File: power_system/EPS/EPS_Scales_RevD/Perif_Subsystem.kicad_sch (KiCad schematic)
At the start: 43 parts, among them CN1 DF11-16DP-2DSA(08), U12 TPS1HB08BQPWPRQ1, U13 LT8612EUDE#PBF, U16 INA260AIPWR

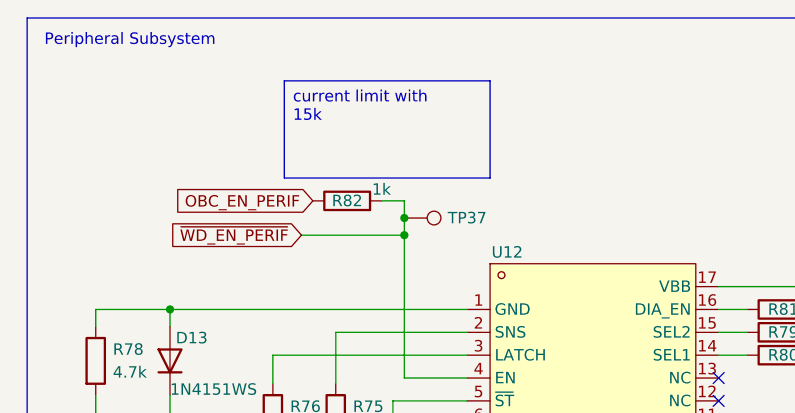
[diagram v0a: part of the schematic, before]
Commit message: Updated Project History
RevA through RevD directly accessible to see project revisions
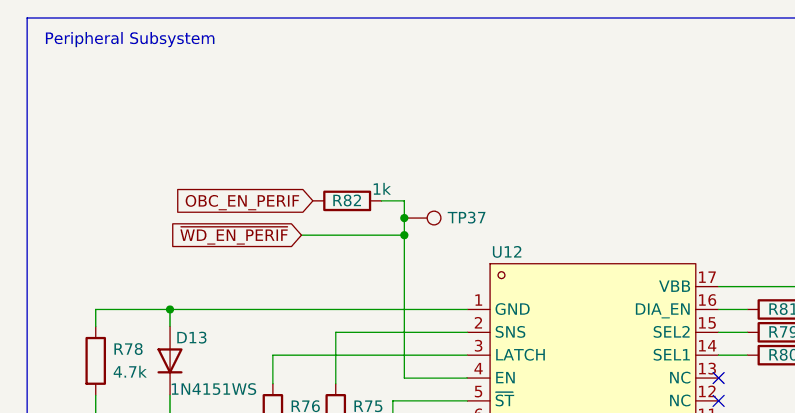
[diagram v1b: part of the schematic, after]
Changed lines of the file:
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@@
 		)
 	)
-	(text_box "current limit with 15k"
-		(exclude_from_sim no)
-		(at 42.545 21.59 0)
-		(size 22.86 10.795)
-		(margins 0.9525 0.9525 0.9525 0.9525)
-		(stroke
-			(width 0)
-			(type solid)
-		)
-		(fill
-			(type none)
-		)
-		(effects
-			(font
-				(size 1.27 1.27)
-			)
-			(justify left top)
-		)
-	)
 	(text_box "R83 and R101 set UVLO @ 24v"
 		(exclude_from_sim no)
@@
 			"eHVFRERlSFE1NVdhSWl6WHRWY1BROEFTeklWcmprdnkzRm9rd1RxM0J0UGtPZGZuZ2cwQm1kLy8r"
 			"S2lSSmZwR0YvTHBIVnl3elNtcGNQM0V2cHdvbDV5cERZNkVrcWhidm5aL2V6aVVvWGUwWDYvVGlw"
-			"dWVYZHlQekJCdw=="
+			"dWVYZHlQekJCd2tQT0dUdFJOWmVBSHI1bk55RE1KVm3gUaSUeVwIgGIrSEdhOXJWaWJ2cE5HNWJQ"
+			"WFBLcWN4bf5RppR5XQiAVmZDaUFxV1NVRTBoVWdCQUd1c0Z1blJo/FG4lGFeCIBuVTJEcHQ5U3ZM"
+			"QkFacHlLZktrc2NxTm76UbqUWl8IgHltbEJtZjNJRlNvRzljeUlBcXd3VE1wVPhRvJR4YAiATlZh"
+			"andFQVY2WVYwNE1vSUlvclBaN0ZC9lG+lHJhCIBsSGZlKzRod2VJTFl4QmdXaDVkRkMrVlX0UbCU"
+			"WWIIgGlxOTJKcFVPRTcyaEtJbDBHcWZMcFIyWPJRspRZYwiAUm5WbE9lOXQyc3A0YUNubEZlVWFL"
+			"S3V08FG0lEtkCIBHSUdFdmtKU3M3N1FnUnFWV2Nta0V1VFTOUbaUVGUIgHMrQndsOUhiZlZST1Jl"
+			"YUx6NGw2RHZUVsxRiJRhZgiAZXNCanJLSXNCYXowNjlMMzF0UnZ2L0JkylGKlG5nCIBZL1U2TERX"
+			"TStxZUV3WU5PclJ6TTZJQ1fIUYyUamgIgFM2ZC9vQ24xZlZKdEdZcmVOd0E3ZFQrecZRjpRPaQiA"
+			"SWl3QnJrQzJxL256WS9ldzRaay9BWkNNxFGAlHFqCIBaL09aaVNtV0QzK1BWYkpZRU1RRURJNFfC"
+			"UYKUUmsIgGs1WVJDOTB0UkYwSEVIVWZEUWJLSmdkecBRhJRXbAiATXhrUnMxWHBqNmpESDVMWnBt"
+			"bGMxYzhK3lGGlFltCIBmU2kwcXRPdDI2UitEcENpc2NJWVpieTbcUZiUaG4IgGNINjAvZm83NlVw"
+			"OVRKZHVOSVJndDFOY9pRmpQrbwiAL2FUWksvZ25BYXhiYi8zcDNqVy92dW5W2FGclDhwCIB1ODZB"
+			"MUNoKzE0ZGdzNEJqakx2LytnZk/WUZ6UL3EIgExGMjBrTGNYTFFRZ0V6eklrMzM5REFXRNRRkJRQ"
+			"cgiAZGpSR3ZjL0hrdm1WaElPRFJLTVJUQU1P0lGSlGpzCIBOaVNiVHdKaTNrZncySEZvcmtEcW1J"
+			"azBQQVlaa2V2dnU0ZUgxNS9MV1B3SS8vcmtNK3hKcENHZlkzYmJhcjY0ckZhdVZJdG5rTVJSMmF4"
+			"VE1RamR0WFVMWjV5OGdxVUw1ckwzdzFkSjlHOWpQQzdRV3VNaVBES0VEY2dIRHhBZmw3K3hVY0JL"
+			"SDl0ZmY1SndMRTRtR3FIL2VBOG1leHR6WjdkeTNwSU9ubmd4Z1JDTmNmKzdUMUlmQ2RGdmROSTEv"
+			"bWdWWVo4VXo0UGJpekRhVGRmZTNjeXVXVXVESzhuYnp6OUczODdYcUtoU2pNTWljbm93b0tSQm9z"
+			"R1BNTGxxaWZaUA=="
 		)
 	)
@@
 		)
 		(instances
-			(project "EPS_Scales_RevC"
+			(project "EPS_Scales_RevD"
 				(path "/f3bdc9b1-4369-4cfa-b765-d952bf408a7b/364fa580-df87-4e65-a29c-42f81b57f892"
 					(page "7")

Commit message: Lots of Goodies
Updated Con. Ops
Updated Footprint Assignments for R and C, WIP
Fixed Incorrect Resistor Values
Updated footprints for LEDs
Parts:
- removed D13: 1N4151WS, symbol EPS:1N4151WS
- added D15: BAS21,215, EPS:SOT-23-3_L2.9-W1.6-P1.90-LS2.8-BR, symbol EPS:BAS21,215
- C36, C38, C39, C49, C51: footprint (none) -> EPS:C0402
- C40, C41, C50: value 0.1u -> 100n; footprint (none) -> EPS:C0402
- D9: footprint (none) -> EPS:LED0603-RD_RED
- R101, R102, R103, R104, R73, R74, R75, R76, R77, R78, R79, R80, R81, R83: footprint (none) -> EPS:R0402
- R82: value 1k -> 15k; footprint (none) -> EPS:R0402
- TP16, TP17, TP18, TP19, TP20, TP21: footprint (none) -> TestPoint:TestPoint_Pad_1.0x1.0mm
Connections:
- net GND: now also D15.3
- net at R78.1, U12.1 (GND): now also D15.1
- no-connect marks 6 -> 7

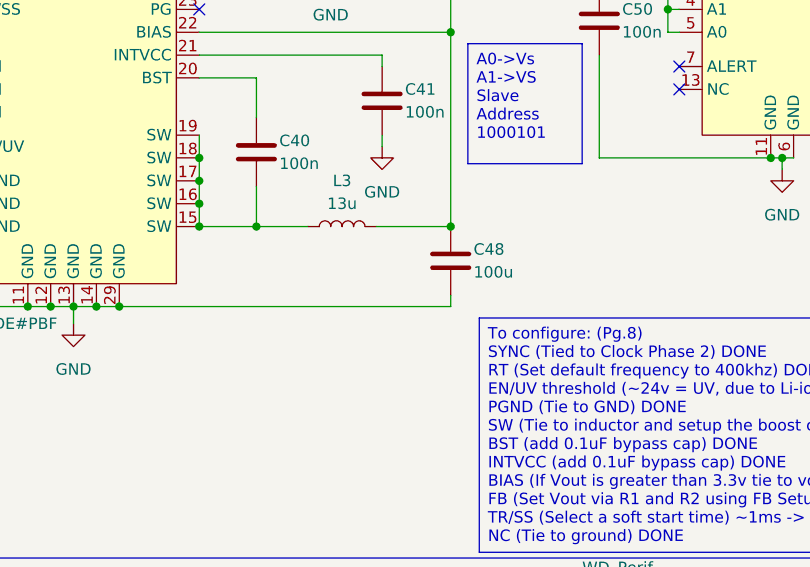
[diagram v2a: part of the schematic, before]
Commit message: More Goodies
Updated Inductor footprints with most readily available LCSC counterparts
Updated XT-60 connector
Updated Edge-Cuts board size
Updated Diode Footprints to fix DRC errors
Started Board layout and copper fills for power and ground
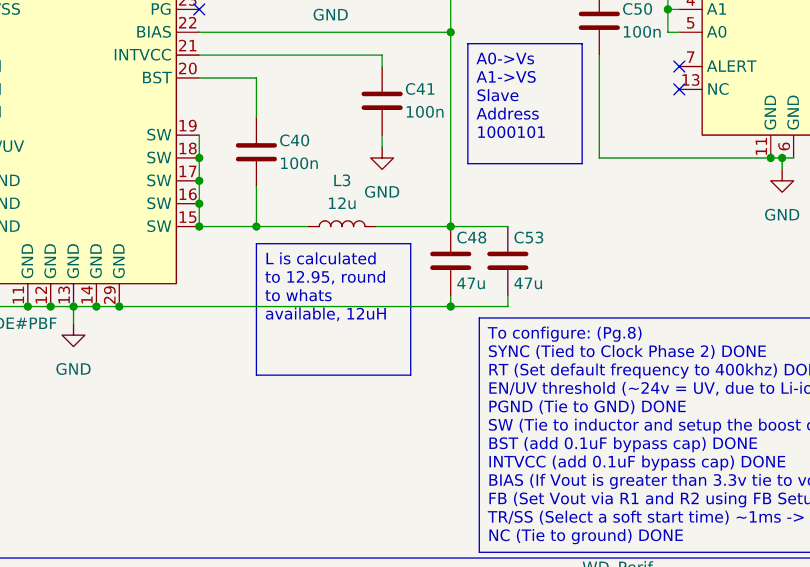
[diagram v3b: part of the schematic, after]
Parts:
- added C53: 47u, EPS:CAP-SMD_L7.3-W4.3-FD, symbol Device:C
- C48: value 100u -> 47u; footprint (none) -> EPS:CAP-SMD_L7.3-W4.3-FD
- L3: value 13u -> 12u; footprint (none) -> EPS:IND-SMD_L13.5-W12.6; LCSC (none) -> C5339468
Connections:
- net GND: now also C53.2
- net at C48.1, C49.1, L3.2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: now also C53.1
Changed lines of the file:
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@@
 		)
 	)
+	(text_box "L is calculated to 12.95, round to whats available, 12uH"
+		(exclude_from_sim no)
+		(at 185.42 73.025 0)
+		(size 17.145 14.605)
+		(margins 0.9525 0.9525 0.9525 0.9525)
+		(stroke
+			(width 0)
+			(type solid)
+		)
+		(fill
+			(type none)
+		)
+		(effects
+			(font
+				(size 1.27 1.27)
+			)
+			(justify left top)
+		)
+	)
 	(text_box "Vbatt = [24.0, 28.8, 33.6] Due to Li-ion battery charged and discharged states"
 		(exclude_from_sim no)
@@
 	)
 	(junction
-		(at 207.01 71.12)
-		(diameter 0)
-		(color 0 0 0 0)
-	)
-	(junction
 		(at 242.57 63.5)
 		(diameter 0)
@@
 	)
 	(junction
+		(at 207.01 80.01)
+		(diameter 0)
+		(color 0 0 0 0)
+	)
+	(junction
 		(at 45.085 140.97)
 		(diameter 0)
@@
 	)
 	(junction
+		(at 207.01 71.12)
+		(diameter 0)
+		(color 0 0 0 0)
+	)
+	(junction
 		(at 223.52 44.45)
 		(diameter 0)
@@
 	(wire
 		(pts
+			(xy 207.01 71.12) (xy 213.36 71.12)
+		)
+		(stroke
+			(width 0)
+			(type default)
+		)
+	)
+	(wire
+		(pts
 			(xy 221.615 44.45) (xy 223.52 44.45)
 		)
@@
 	(wire
 		(pts
+			(xy 207.01 80.01) (xy 213.36 80.01)
+		)
+		(stroke
+			(width 0)
+			(type default)
+		)
+	)
+	(wire
+		(pts
+			(xy 213.36 80.01) (xy 213.36 78.74)
+		)
+		(stroke
+			(width 0)
+			(type default)
+		)
+	)
+	(wire
+		(pts
 			(xy 149.86 44.45) (xy 151.13 44.45)
 		)
@@
 	)
 	(symbol
+		(lib_id "Device:C")
+		(at 207.01 74.93 0)
+		(unit 1)
+		(exclude_from_sim no)
+		(in_bom yes)
+		(on_board yes)
+		(dnp no)
+		(property "Reference" "C48"
+			(at 207.645 72.39 0)
+			(effects
+				(font
+					(size 1.27 1.27)
+				)
+				(justify left)
+			)
+		)
+		(property "Value" "47u"
+			(at 207.645 77.47 0)
+			(effects
+				(font
+					(size 1.27 1.27)
+				)
+				(justify left)
+			)
+		)
+		(property "Footprint" "EPS:CAP-SMD_L7.3-W4.3-FD"
+			(at 207.9752 78.74 0)
+			(effects
+				(font
+					(size 1.27 1.27)
+				)
+				(hide yes)
+			)
+		)
+		(property "Datasheet" "~"
+			(at 207.01 74.93 0)
+			(effects
+				(font
+					(size 1.27 1.27)
+				)
+				(hide yes)
+			)
+		)
+		(property "Description" "Unpolarized capacitor"
+			(at 207.01 74.93 0)
+			(effects
+				(font
+					(size 1.27 1.27)
+				)
+				(hide yes)
+			)
+		)
+		(pin "1"
+		)
+		(pin "2"
+		)
+		(instances
+			(project "EPS_Scales_RevD"
+				(path "/f3bdc9b1-4369-4cfa-b765-d952bf408a7b/364fa580-df87-4e65-a29c-42f81b57f892"
+					(reference "C48")
+					(unit 1)
+				)
+			)
+		)
+	)
+	(symbol
 		(lib_id "Device:R")
 		(at 145.415 66.04 0)
@@
 	)
 	(symbol
+		(lib_id "Device:C")
+		(at 213.36 74.93 0)
+		(unit 1)
+		(exclude_from_sim no)
+		(in_bom yes)
+		(on_board yes)
+		(dnp no)
+		(property "Reference" "C53"
+			(at 213.995 72.39 0)
+			(effects
+				(font
+					(size 1.27 1.27)
+				)
+				(justify left)
+			)
+		)
+		(property "Value" "47u"
+			(at 213.995 77.47 0)
+			(effects
+				(font
+					(size 1.27 1.27)
+				)
+				(justify left)
+			)
+		)
+		(property "Footprint" "EPS:CAP-SMD_L7.3-W4.3-FD"
+			(at 214.3252 78.74 0)
+			(effects
+				(font
+					(size 1.27 1.27)
+				)
+				(hide yes)
+			)
+		)
+		(property "Datasheet" "~"
+			(at 213.36 74.93 0)
+			(effects
+				(font
+					(size 1.27 1.27)
+				)
+				(hide yes)
+			)
+		)
+		(property "Description" "Unpolarized capacitor"
+			(at 213.36 74.93 0)
+			(effects
+				(font
+					(size 1.27 1.27)
+				)
+				(hide yes)
+			)
+		)
+		(pin "1"
+		)
+		(pin "2"
+		)
+		(instances
+			(project "EPS_Scales_RevD"
+				(path "/f3bdc9b1-4369-4cfa-b765-d952bf408a7b/364fa580-df87-4e65-a29c-42f81b57f892"
+					(reference "C53")
+					(unit 1)
+				)
+			)
+		)
+	)
+	(symbol
 		(lib_id "Connector:TestPoint")
 		(at 100.33 64.135 0)
@@
 	)
 	(symbol
-		(lib_id "Device:C")
-		(at 207.01 74.93 0)
-		(unit 1)
-		(exclude_from_sim no)
-		(in_bom yes)
-		(on_board yes)
-		(dnp no)
-		(property "Reference" "C48"
-			(at 209.55 73.66 0)
-			(effects
-				(font
-					(size 1.27 1.27)
-				)
-				(justify left)
-			)
-		)
-		(property "Value" "100u"
-			(at 209.55 76.2 0)
-			(effects
-				(font
-					(size 1.27 1.27)
-				)
-				(justify left)
-			)
-		)
-		(property "Footprint" ""
-			(at 207.9752 78.74 0)
-			(effects
-				(font
-					(size 1.27 1.27)
-				)
-				(hide yes)
-			)
-		)
-		(property "Datasheet" "~"
-			(at 207.01 74.93 0)
-			(effects
-				(font
-					(size 1.27 1.27)
-				)
-				(hide yes)
-			)
-		)
-		(property "Description" "Unpolarized capacitor"
-			(at 207.01 74.93 0)
-			(effects
-				(font
-					(size 1.27 1.27)
-				)
-				(hide yes)
-			)
-		)
-		(pin "2"
-		)
-		(pin "1"
-		)
-		(instances
-			(project "EPS_Scales_RevC"
-				(path "/f3bdc9b1-4369-4cfa-b765-d952bf408a7b/364fa580-df87-4e65-a29c-42f81b57f892"
-					(reference "C48")
-					(unit 1)
-				)
-			)
-		)
-	)
-	(symbol
 		(lib_id "Connector:TestPoint")
 		(at 60.325 140.97 270)
@@
 			)
 		)
-		(property "Value" "13u"
+		(property "Value" "12u"
 			(at 194.945 68.58 90)
 			(effects
@@
 			)
 		)
-		(property "Footprint" ""
+		(property "Footprint" "EPS:IND-SMD_L13.5-W12.6"
 			(at 194.945 71.12 0)
 			(effects
@@
 			)
 		)
-		(property "Datasheet" "~"
+		(property "Datasheet" "https://www.lcsc.com/datasheet/lcsc_datasheet_2411041754_XR-XR1265-120M_C5339468.pdf"
 			(at 194.945 71.12 0)
 			(effects
@@
 			)
 		)
-		(property "Description" "Inductor"
+		(property "Description" "XR XR1265-120M"
 			(at 194.945 71.12 0)
 			(effects
 				(font
+					(size 1.27 1.27)
+				)
+				(hide yes)
+			)
+		)
+		(property "LCSC" "C5339468"
+			(at 194.945 71.12 90)
+			(effects
+				(font

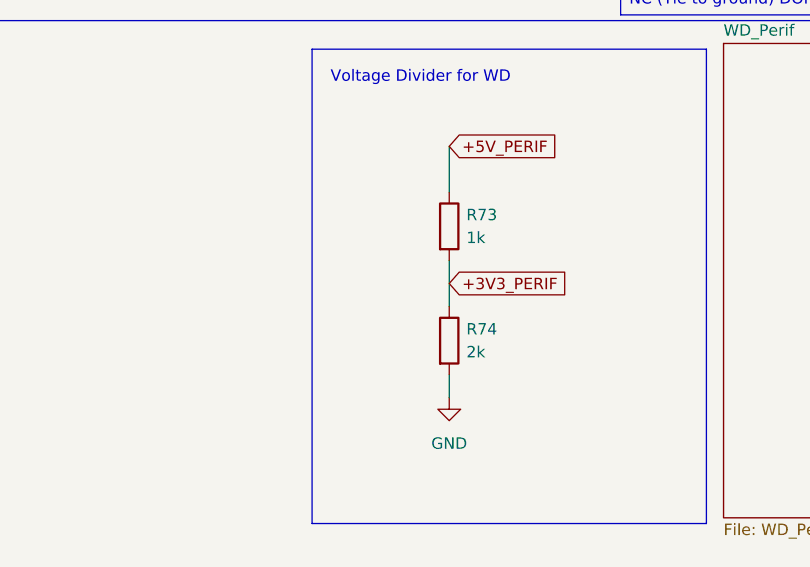
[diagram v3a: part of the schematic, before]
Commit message: Board Layout complete
Its a bit messy but I think ive managed to get the loop areas small enough, and the board to represent what is on the schematic. Probably would be a good idea to get a look at it from someone more reputable than myself on how this board should be layed out.
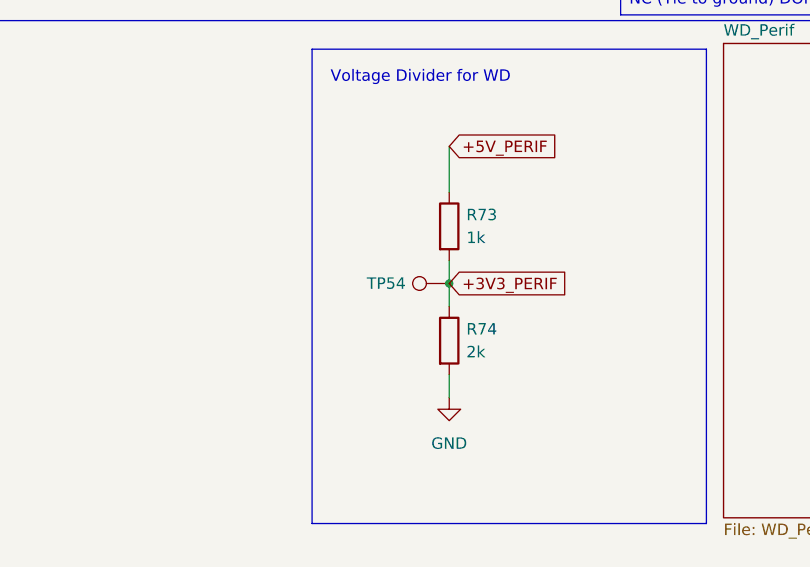
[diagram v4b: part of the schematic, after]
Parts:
- added TP54: TestPoint, TestPoint:TestPoint_Pad_1.0x1.0mm, symbol Connector:TestPoint
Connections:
- net +3V3_PERIF: now also TP54.1
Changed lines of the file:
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@@
 	)
 	(junction
+		(at 191.135 137.16)
+		(diameter 0)
+		(color 0 0 0 0)
+	)
+	(junction
 		(at 45.085 140.97)
 		(diameter 0)
@@
 	(wire
 		(pts
-			(xy 191.135 134.62) (xy 191.135 139.7)
+			(xy 191.135 134.62) (xy 191.135 137.16)
 		)
 		(stroke
@@
 	(wire
 		(pts
+			(xy 191.135 137.16) (xy 191.135 139.7)
+		)
+		(stroke
+			(width 0)
+			(type default)
+		)
+	)
+	(wire
+		(pts
 			(xy 145.415 53.34) (xy 151.13 53.34)
 		)
@@
 					(unit 1)
 				)
+			)
+		)
+	)
+	(symbol
+		(lib_id "Connector:TestPoint")
+		(at 191.135 137.16 90)
+		(unit 1)
+		(exclude_from_sim no)
+		(in_bom yes)
+		(on_board yes)
+		(dnp no)
+		(property "Reference" "TP54"
+			(at 186.309 137.16 90)
+			(effects
+				(font
+					(size 1.27 1.27)
+				)
+				(justify left)
+			)
+		)
+		(property "Value" "TestPoint"
+			(at 186.055 135.8901 90)
+			(effects
+				(font
+					(size 1.27 1.27)
+				)
+				(justify left)
+				(hide yes)
+			)
+		)
+		(property "Footprint" "TestPoint:TestPoint_Pad_1.0x1.0mm"
+			(at 191.135 132.08 0)
+			(effects
+				(font
+					(size 1.27 1.27)
+				)
+				(hide yes)
+			)
+		)
+		(property "Datasheet" "~"
+			(at 191.135 132.08 0)
+			(effects
+				(font
+					(size 1.27 1.27)
+				)
+				(hide yes)
+			)
+		)
+		(property "Description" "test point"
+			(at 191.135 137.16 0)
+			(effects
+				(font
+					(size 1.27 1.27)
+				)
+				(hide yes)
+			)
+		)
+		(pin "1"
+		)
+		(instances
+			(project "EPS_Scales_RevD"
+				(path "/f3bdc9b1-4369-4cfa-b765-d952bf408a7b/364fa580-df87-4e65-a29c-42f81b57f892"
+					(reference "TP54")
+					(unit 1)
+				)
